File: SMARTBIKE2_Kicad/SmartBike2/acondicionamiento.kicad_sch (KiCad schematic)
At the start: 1 part, among them IC1 ESP32-WROVER-B__8MB_

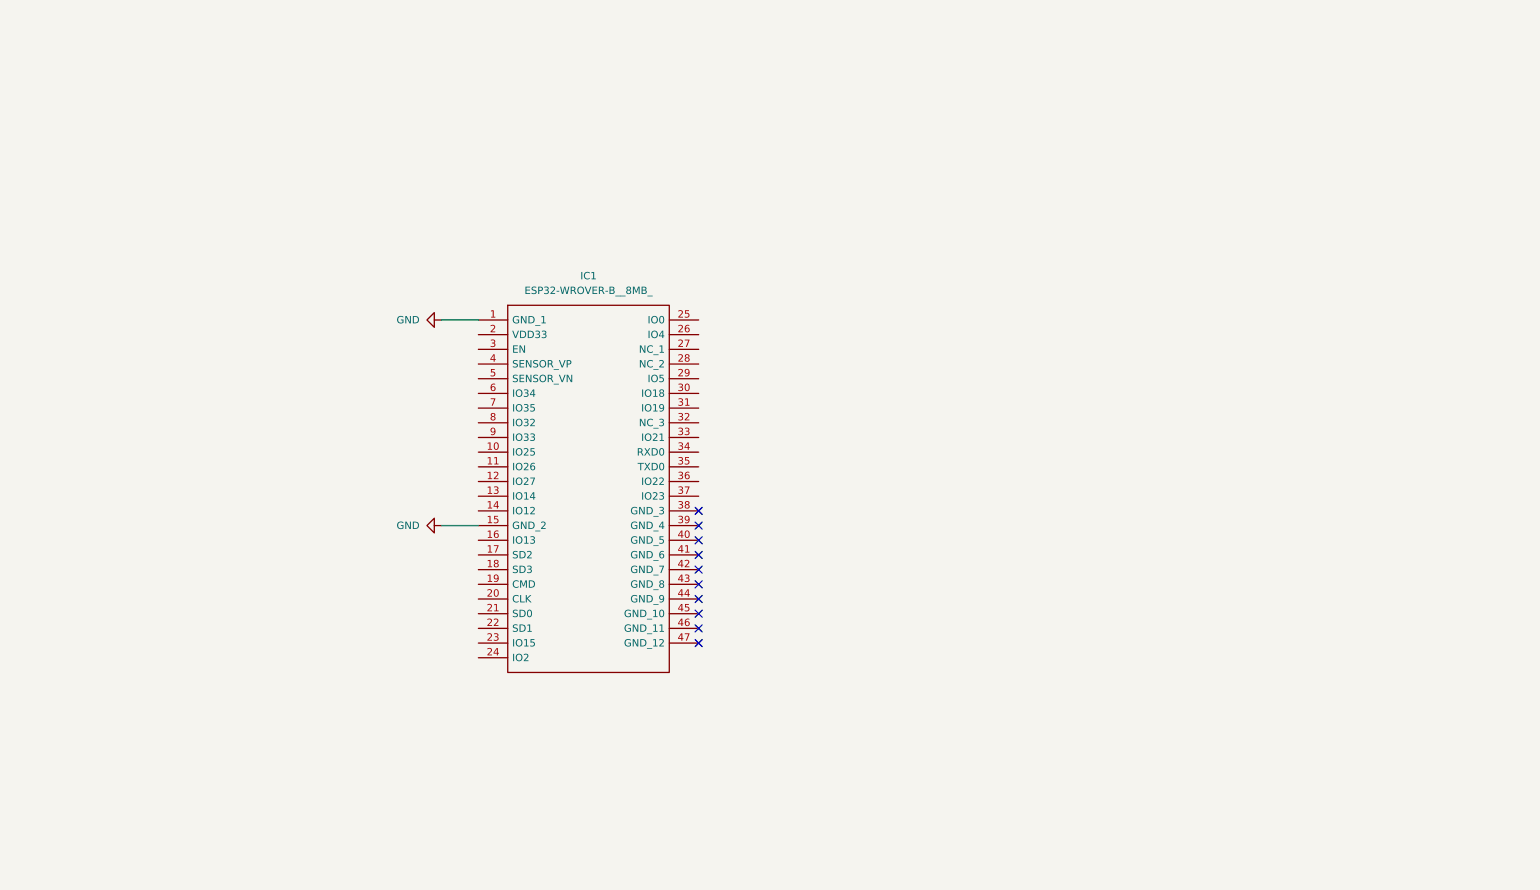
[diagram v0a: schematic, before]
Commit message: Beta 100% esquemáticos
+ Acondicionamiento ESP32

~ Huellas
~ PCB
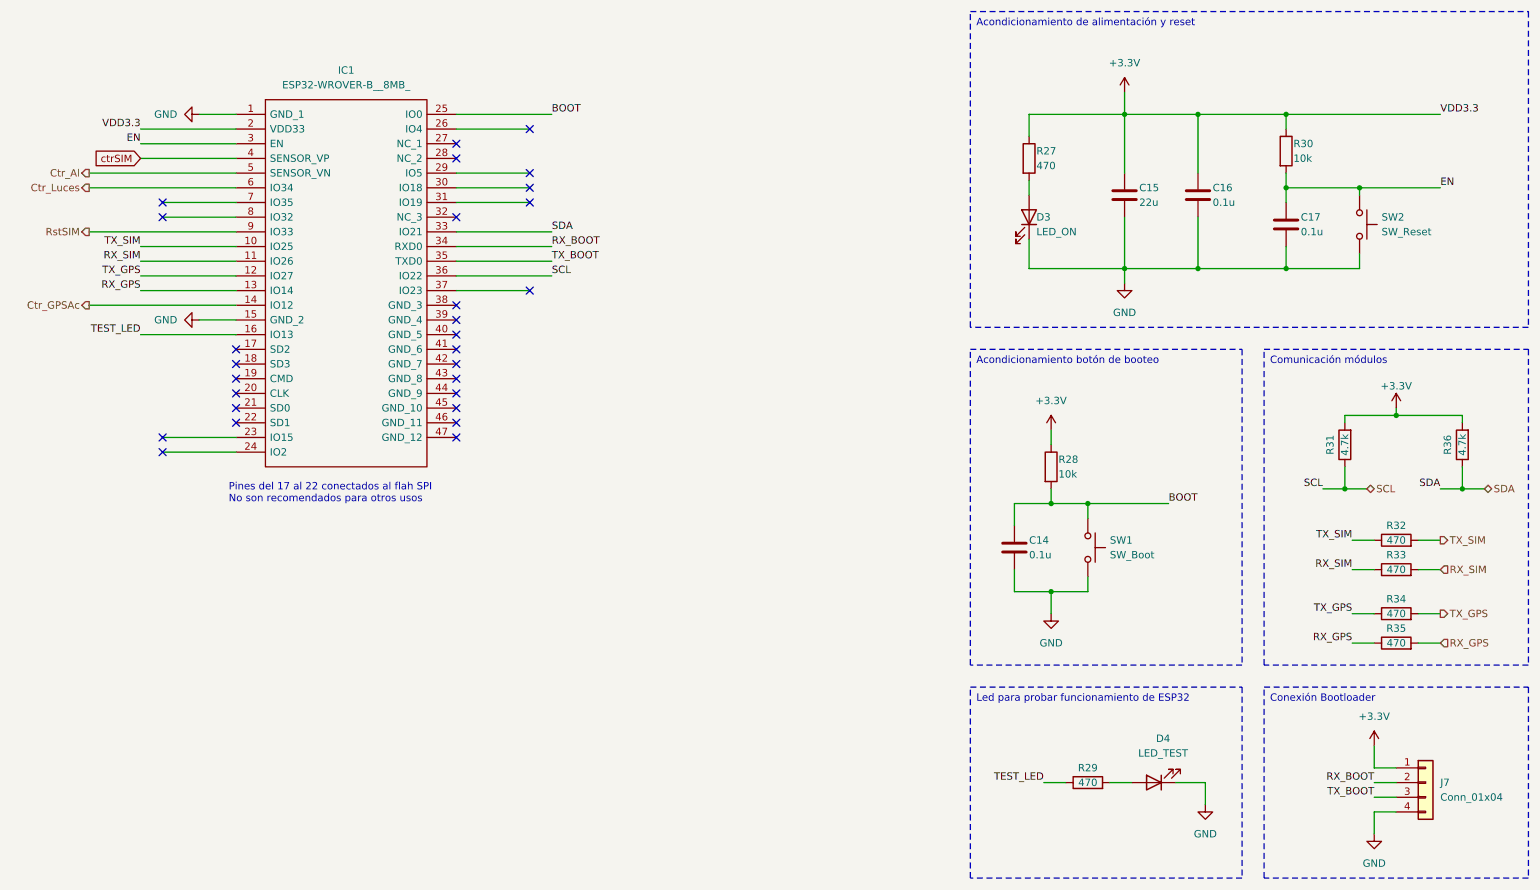
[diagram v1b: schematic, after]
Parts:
- added C14, C16, C17: 0.1u, symbol Device:C
- added C15: 22u, symbol Device:C
- added D3: LED_ON, symbol Device:LED
- added D4: LED_TEST, symbol Device:LED
- added J7: Conn_01x04, symbol Connector_Generic:Conn_01x04
- added R27, R29, R32, R33, R34, R35: 470, symbol Device:R
- added R28, R30: 10k, symbol Device:R
- added R31, R36: 4.7k, symbol Device:R
- added SW1: SW_Boot, symbol Switch:SW_Push
- added SW2: SW_Reset, symbol Switch:SW_Push
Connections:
- net GND: now also C14.2, C15.2, C16.2, C17.2, D3.1 (K), D4.1 (K), J7.4 (Pin_4), SW1.1, SW2.2
- net TX_SIM: now reaches IC1.10 (IO25)
- net TX_SIM: now also R32.1, R32.2
- net RX_SIM: now reaches IC1.11 (IO26)
- net RX_SIM: now also R33.1, R33.2
- net TX_GPS: now reaches IC1.12 (IO27)
- net TX_GPS: now also R34.1, R34.2
- net RX_GPS: now reaches IC1.13 (IO14)
- net RX_GPS: now also R35.1, R35.2
- net Ctr_GPSAc: now reaches IC1.14 (IO12)
- net TEST_LED: now reaches IC1.16 (IO13)
- net TEST_LED: now also R29.1
- net +3.3V: now reaches IC1.2 (VDD33)
- net +3.3V: now also C15.1, C16.1, J7.1 (Pin_1), R27.1, R28.1, R30.1, R31.2, R36.2
- net BOOT: now reaches IC1.25 (IO0)
- net BOOT: now also C14.1, R28.2, SW1.2
- net EN: now reaches IC1.3 (EN)
- net EN: now also C17.1, R30.2, SW2.1
- net SDA: now reaches IC1.33 (IO21)
- net SDA: now also R36.1
- net RX_BOOT: now reaches IC1.34 (RXD0)
- net RX_BOOT: now also J7.2 (Pin_2)
- net TX_BOOT: now reaches IC1.35 (TXD0)
- net TX_BOOT: now also J7.3 (Pin_3)
- net SCL: now reaches IC1.36 (IO22)
- net SCL: now also R31.1
- net ctrSIM: now reaches IC1.4 (SENSOR_VP)
- net Ctr_Al: now reaches IC1.5 (SENSOR_VN)
- net Ctr_Luces: now reaches IC1.6 (IO34)
- net RstSIM: now reaches IC1.9 (IO33)
- new net: D4.2 (A), R29.2
- new net: D3.2 (A), R27.2
- no-connect marks 10 -> 28
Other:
- note added: "Pines del 17 al 22 conectados al flah SPI No son recomendados para otros usos"
- moved on the sheet: IC1

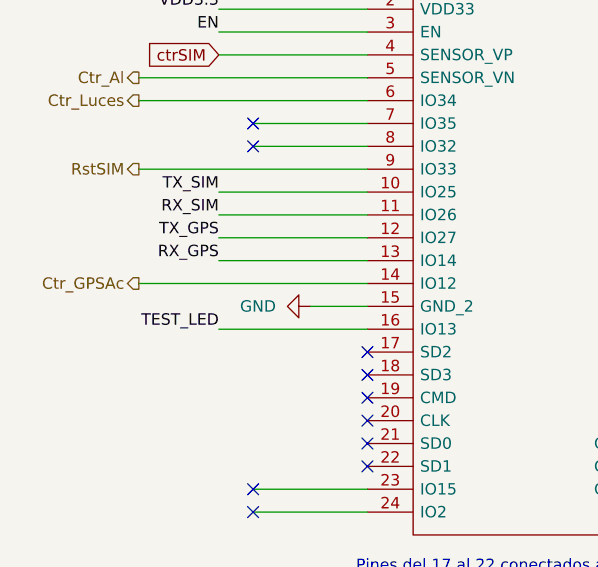
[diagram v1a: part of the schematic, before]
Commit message: cambio alimentacion GPS
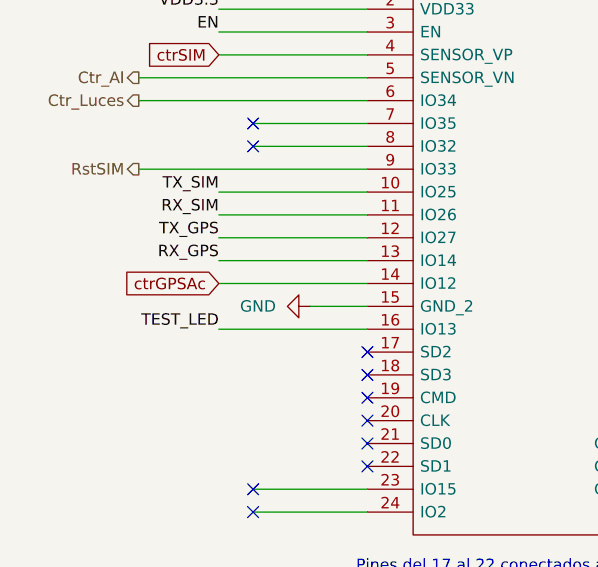
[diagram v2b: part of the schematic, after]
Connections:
- net Ctr_GPSAc renamed ctrGPSAc
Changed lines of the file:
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@@
-    (stroke (width 0) (type default))
-  )
-  (wire (pts (xy 25.4 63.5) (xy 50.8 63.5))
     (stroke (width 0) (type default))
   )
@@
   )
   (wire (pts (xy 243.84 109.22) (xy 247.65 109.22))
+    (stroke (width 0) (type default))
+  )
+  (wire (pts (xy 34.29 63.5) (xy 50.8 63.5))
     (stroke (width 0) (type default))
   )
@@
   (label "TX_SIM" (at 243.84 104.14 180) (fields_autoplaced)
     (effects (font (size 1.27 1.27)) (justify right bottom))
+  )
+  (global_label "ctrGPSAc" (shape input) (at 34.29 63.5 180) (fields_autoplaced)
+    (effects (font (size 1.27 1.27)) (justify right))
+    (property "Intersheetrefs" "${INTERSHEET_REFS}" (at 22.7776 63.5 0)
+      (effects (font (size 1.27 1.27)) (justify right) hide)
+    )
   )
   (global_label "ctrSIM" (shape input) (at 34.29 38.1 180) (fields_autoplaced)
@@
     (effects (font (size 1.27 1.27)) (justify left))
   )
-  (hierarchical_label "Ctr_GPSAc" (shape output) (at 25.4 63.5 180) (fields_autoplaced)
-    (effects (font (size 1.27 1.27)) (justify right))
-  )
   (hierarchical_label "Ctr_Al" (shape output) (at 25.4 40.64 180) (fields_autoplaced)

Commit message: cache
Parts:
- C14, C15, C16, C17: footprint (none) -> Capacitor_SMD:C_0805_2012Metric_Pad1.18x1.45mm_HandSolder
- D3, D4: footprint (none) -> LED_SMD:LED_1206_3216Metric_Pad1.42x1.75mm_HandSolder
- IC1: footprint ESP32WROVERB8MB -> ESP32-WROVER-B__8MB_:ESP32WROVERB8MB
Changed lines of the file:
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@@
       (effects (font (size 1.27 1.27)) (justify left))
     )
-    (property "Footprint" "" (at 205.4352 48.26 0)
+    (property "Footprint" "Capacitor_SMD:C_0805_2012Metric_Pad1.18x1.45mm_HandSolder" (at 205.4352 48.26 0)
       (effects (font (size 1.27 1.27)) hide)
     )
@@
       (effects (font (size 1.27 1.27)) (justify left))
     )
-    (property "Footprint" "" (at 218.1352 48.26 0)
+    (property "Footprint" "Capacitor_SMD:C_0805_2012Metric_Pad1.18x1.45mm_HandSolder" (at 218.1352 48.26 0)
       (effects (font (size 1.27 1.27)) hide)
     )
@@
       (effects (font (size 1.27 1.27)))
     )
-    (property "Footprint" "" (at 209.55 146.05 0)
+    (property "Footprint" "LED_SMD:LED_1206_3216Metric_Pad1.42x1.75mm_HandSolder" (at 209.55 146.05 0)
       (effects (font (size 1.27 1.27)) hide)
     )
@@
       (effects (font (size 1.27 1.27)) (justify left))
     )
-    (property "Footprint" "" (at 187.96 48.26 0)
+    (property "Footprint" "LED_SMD:LED_1206_3216Metric_Pad1.42x1.75mm_HandSolder" (at 187.96 48.26 0)
       (effects (font (size 1.27 1.27)) hide)
     )
@@
       (effects (font (size 1.27 1.27)) (justify left))
     )
-    (property "Footprint" "" (at 233.3752 53.34 0)
+    (property "Footprint" "Capacitor_SMD:C_0805_2012Metric_Pad1.18x1.45mm_HandSolder" (at 233.3752 53.34 0)
       (effects (font (size 1.27 1.27)) hide)
     )
@@
       (effects (font (size 1.27 1.27)))
     )
-    (property "Footprint" "ESP32WROVERB8MB" (at 85.09 27.94 0)
+    (property "Footprint" "ESP32-WROVER-B__8MB_:ESP32WROVERB8MB" (at 85.09 27.94 0)
       (effects (font (size 1.27 1.27)) (justify left) hide)
     )
@@
       (effects (font (size 1.27 1.27)) (justify left))
     )
-    (property "Footprint" "" (at 186.3852 109.22 0)
-      (effects (font (size 1.27 1.27)) hide)
-    )
+    (property "Footprint" "Capacitor_SMD:C_0805_2012Metric_Pad1.18x1.45mm_HandSolder" (at 186.3852 109.22 0)
+      (effects (font (size 1.27 1.27)) hide)
+    )

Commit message: Mas huellas
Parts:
- R27, R28, R29, R30, R31, R32, R33, R34, R35, R36: footprint (none) -> Resistor_SMD:R_0805_2012Metric_Pad1.20x1.40mm_HandSolder
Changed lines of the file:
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@@
       (effects (font (size 1.27 1.27)))
     )
-    (property "Footprint" "" (at 198.12 147.828 90)
+    (property "Footprint" "Resistor_SMD:R_0805_2012Metric_Pad1.20x1.40mm_HandSolder" (at 198.12 147.828 90)
       (effects (font (size 1.27 1.27)) hide)
     )
@@
       (effects (font (size 1.27 1.27)) (justify left))
     )
-    (property "Footprint" "" (at 186.182 38.1 90)
+    (property "Footprint" "Resistor_SMD:R_0805_2012Metric_Pad1.20x1.40mm_HandSolder" (at 186.182 38.1 90)
       (effects (font (size 1.27 1.27)) hide)
     )
@@
       (effects (font (size 1.27 1.27)))
     )
-    (property "Footprint" "" (at 264.668 87.63 90)
+    (property "Footprint" "Resistor_SMD:R_0805_2012Metric_Pad1.20x1.40mm_HandSolder" (at 264.668 87.63 90)
       (effects (font (size 1.27 1.27)) hide)
     )
@@
       (effects (font (size 1.27 1.27)))
     )
-    (property "Footprint" "" (at 251.46 105.918 90)
+    (property "Footprint" "Resistor_SMD:R_0805_2012Metric_Pad1.20x1.40mm_HandSolder" (at 251.46 105.918 90)
       (effects (font (size 1.27 1.27)) hide)
     )
@@
       (effects (font (size 1.27 1.27)))
     )
-    (property "Footprint" "" (at 251.46 123.698 90)
+    (property "Footprint" "Resistor_SMD:R_0805_2012Metric_Pad1.20x1.40mm_HandSolder" (at 251.46 123.698 90)
       (effects (font (size 1.27 1.27)) hide)
     )
@@
       (effects (font (size 1.27 1.27)) (justify left))
     )
-    (property "Footprint" "" (at 189.992 91.44 90)
+    (property "Footprint" "Resistor_SMD:R_0805_2012Metric_Pad1.20x1.40mm_HandSolder" (at 189.992 91.44 90)
       (effects (font (size 1.27 1.27)) hide)
     )
@@
       (effects (font (size 1.27 1.27)))
     )
-    (property "Footprint" "" (at 251.46 118.618 90)
+    (property "Footprint" "Resistor_SMD:R_0805_2012Metric_Pad1.20x1.40mm_HandSolder" (at 251.46 118.618 90)
       (effects (font (size 1.27 1.27)) hide)
     )
@@
       (effects (font (size 1.27 1.27)))
     )
-    (property "Footprint" "" (at 244.348 87.63 90)
+    (property "Footprint" "Resistor_SMD:R_0805_2012Metric_Pad1.20x1.40mm_HandSolder" (at 244.348 87.63 90)
       (effects (font (size 1.27 1.27)) hide)
     )
@@
       (effects (font (size 1.27 1.27)))
     )
-    (property "Footprint" "" (at 251.46 110.998 90)
+    (property "Footprint" "Resistor_SMD:R_0805_2012Metric_Pad1.20x1.40mm_HandSolder" (at 251.46 110.998 90)
       (effects (font (size 1.27 1.27)) hide)
     )
@@
       (effects (font (size 1.27 1.27)) (justify left))
     )
-    (property "Footprint" "" (at 230.632 36.83 90)
-      (effects (font (size 1.27 1.27)) hide)
-    )
+    (property "Footprint" "Resistor_SMD:R_0805_2012Metric_Pad1.20x1.40mm_HandSolder" (at 230.632 36.83 90)
+      (effects (font (size 1.27 1.27)) hide)
+    )

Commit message: mas huellas
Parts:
- J7: footprint (none) -> Connector_PinSocket_2.54mm:PinSocket_1x04_P2.54mm_Vertical
- SW1, SW2: footprint (none) -> Button_Switch_SMD:SW_SPST_CK_RS282G05A3
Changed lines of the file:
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@@
       (effects (font (size 1.27 1.27)) (justify left))
     )
-    (property "Footprint" "" (at 203.2 105.41 0)
+    (property "Footprint" "Button_Switch_SMD:SW_SPST_CK_RS282G05A3" (at 203.2 105.41 0)
       (effects (font (size 1.27 1.27)) hide)
     )
@@
       (effects (font (size 1.27 1.27)) (justify left))
     )
-    (property "Footprint" "" (at 256.54 146.05 0)
+    (property "Footprint" "Connector_PinSocket_2.54mm:PinSocket_1x04_P2.54mm_Vertical" (at 256.54 146.05 0)
       (effects (font (size 1.27 1.27)) hide)
     )
@@
       (effects (font (size 1.27 1.27)) (justify left))
     )
-    (property "Footprint" "" (at 250.19 49.53 0)
-      (effects (font (size 1.27 1.27)) hide)
-    )
+    (property "Footprint" "Button_Switch_SMD:SW_SPST_CK_RS282G05A3" (at 250.19 49.53 0)
+      (effects (font (size 1.27 1.27)) hide)
+    )
